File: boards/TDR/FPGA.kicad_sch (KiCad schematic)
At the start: 3 parts, among them U1 LFE5UM5G-45-CABGA381

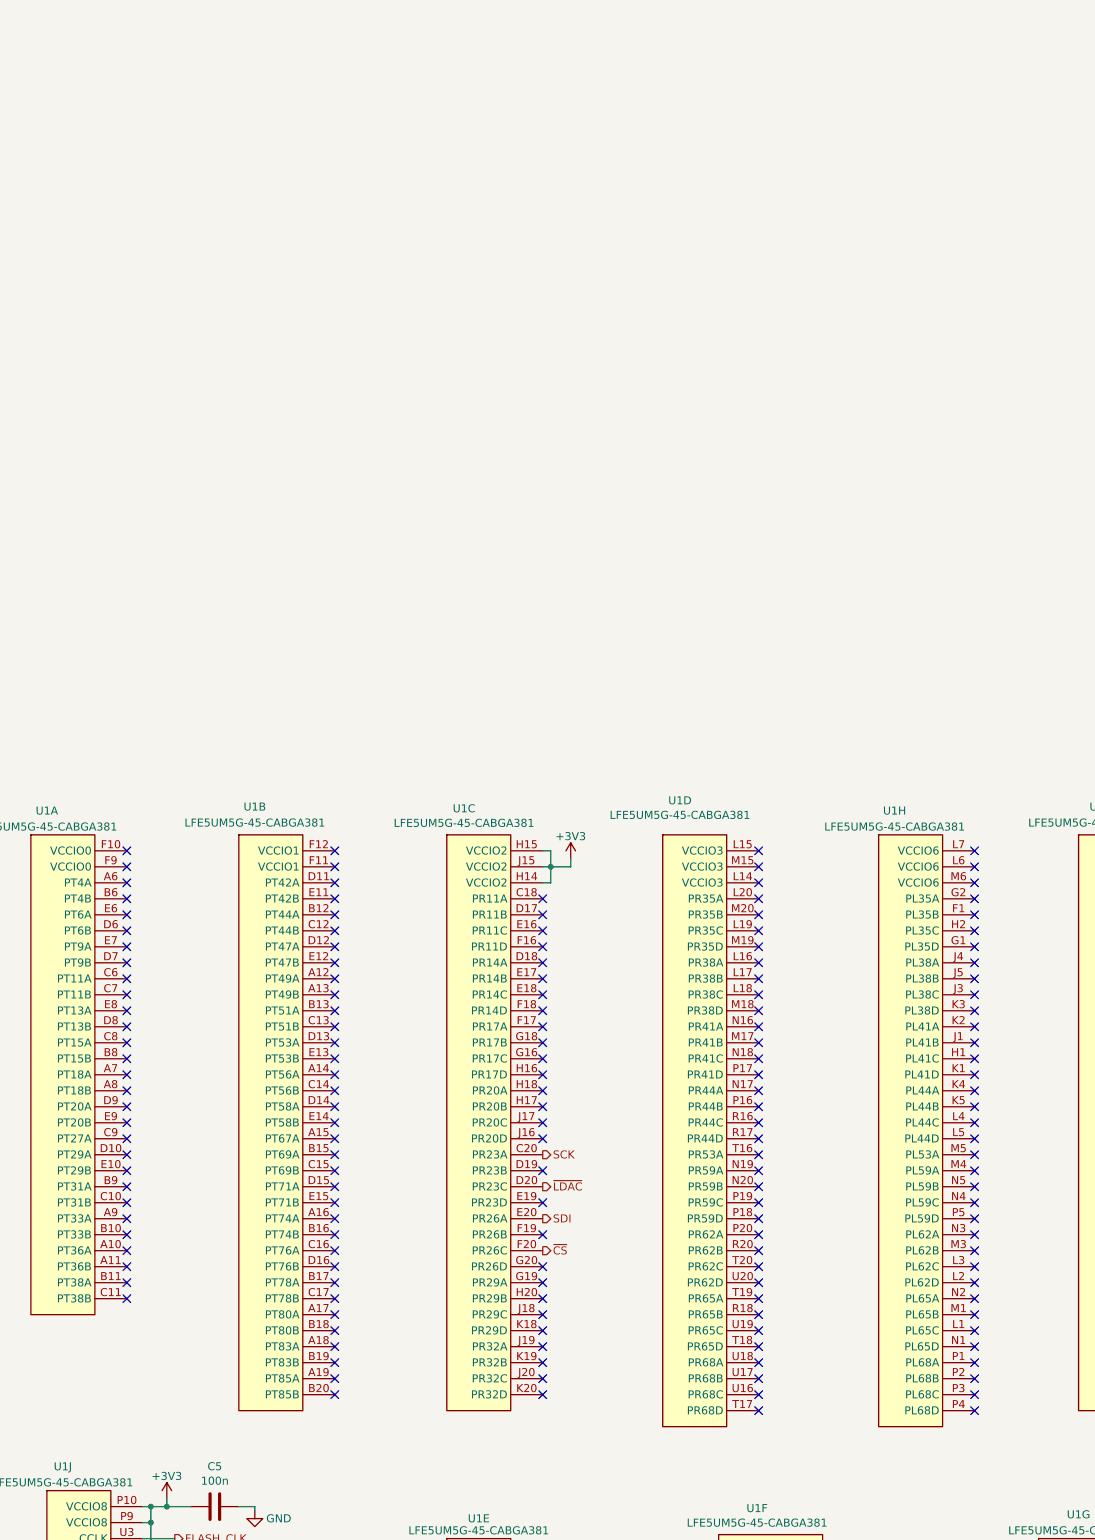
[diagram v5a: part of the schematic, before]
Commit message: add LEDs, only 9 unconnected items remaining
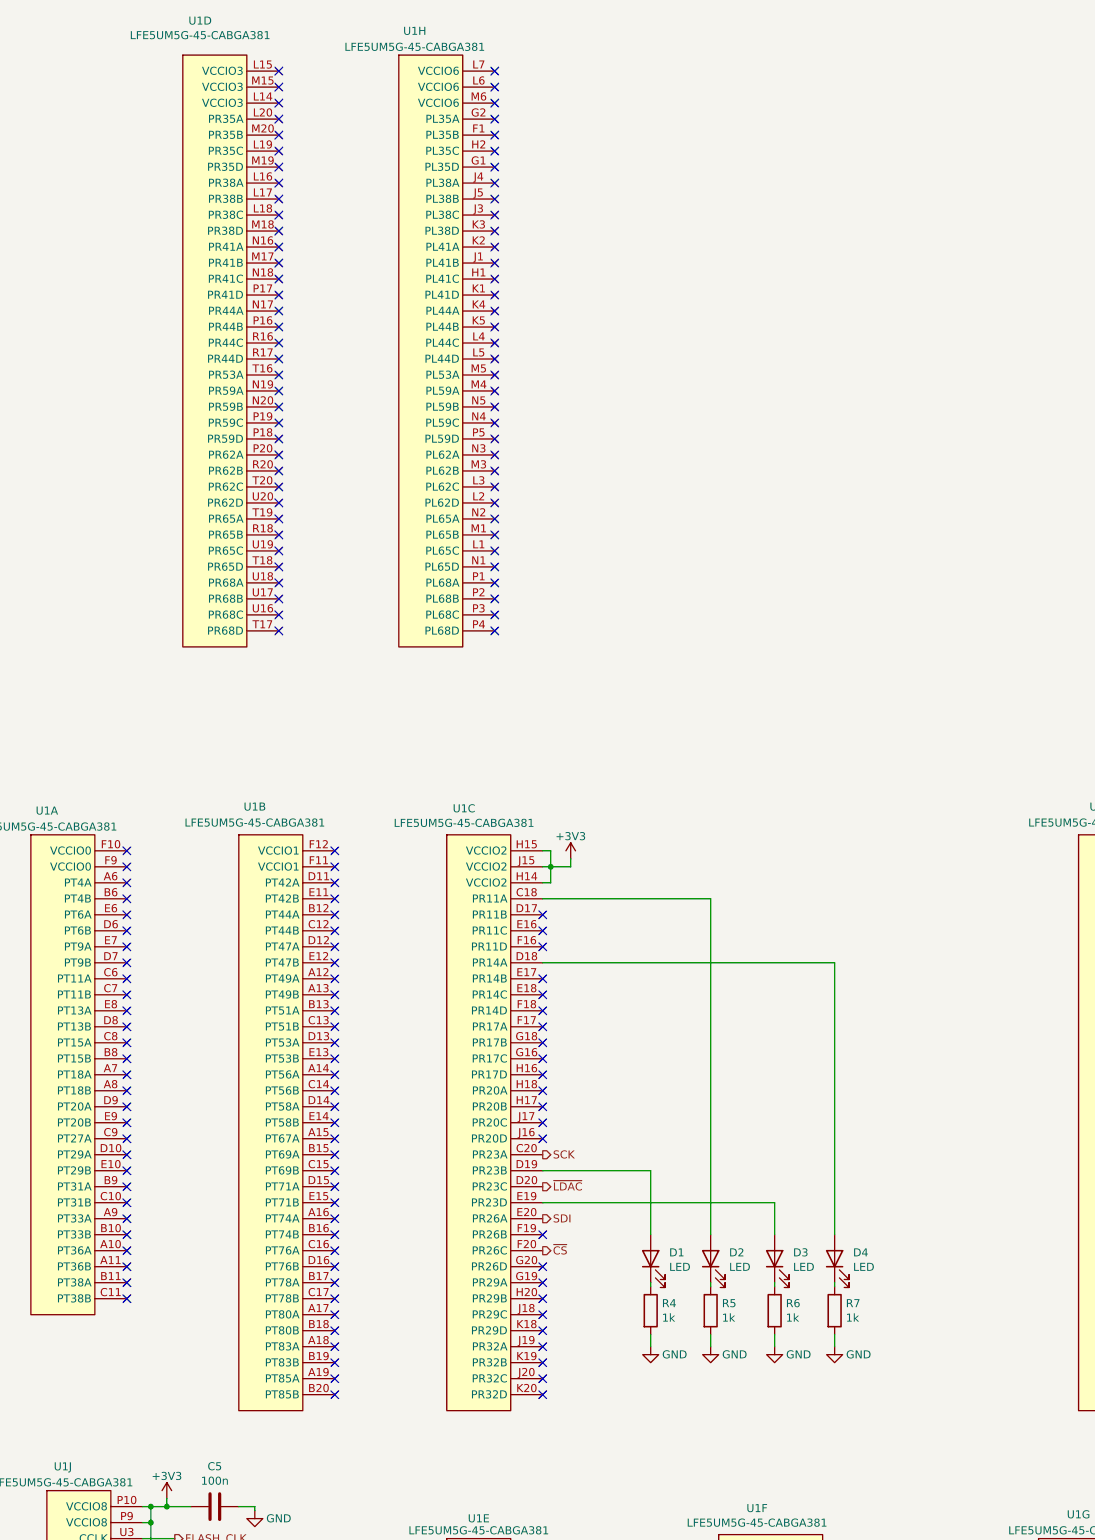
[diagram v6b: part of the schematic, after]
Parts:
- added D1, D2, D3, D4: LED, LED_SMD:LED_0805_2012Metric_Castellated, symbol Device:LED
- added R4, R5, R6, R7: 1k, Resistor_SMD:R_0805_2012Metric, symbol Device:R
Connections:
- net GND: now also R4.2, R5.2, R6.2, R7.2
- net at U1.C18 (PR11A): now also D2.2 (A)
- net at U1.D18 (PR14A): now also D4.2 (A)
- net at U1.D19 (PR23B): now also D1.2 (A)
- net at U1.E19 (PR23D): now also D3.2 (A)
- new net: D2.1 (K), R5.1
- new net: D1.1 (K), R4.1
- new net: D4.1 (K), R7.1
- new net: D3.1 (K), R6.1
- no-connect marks 201 -> 197
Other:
- moved on the sheet: U1D, U1H

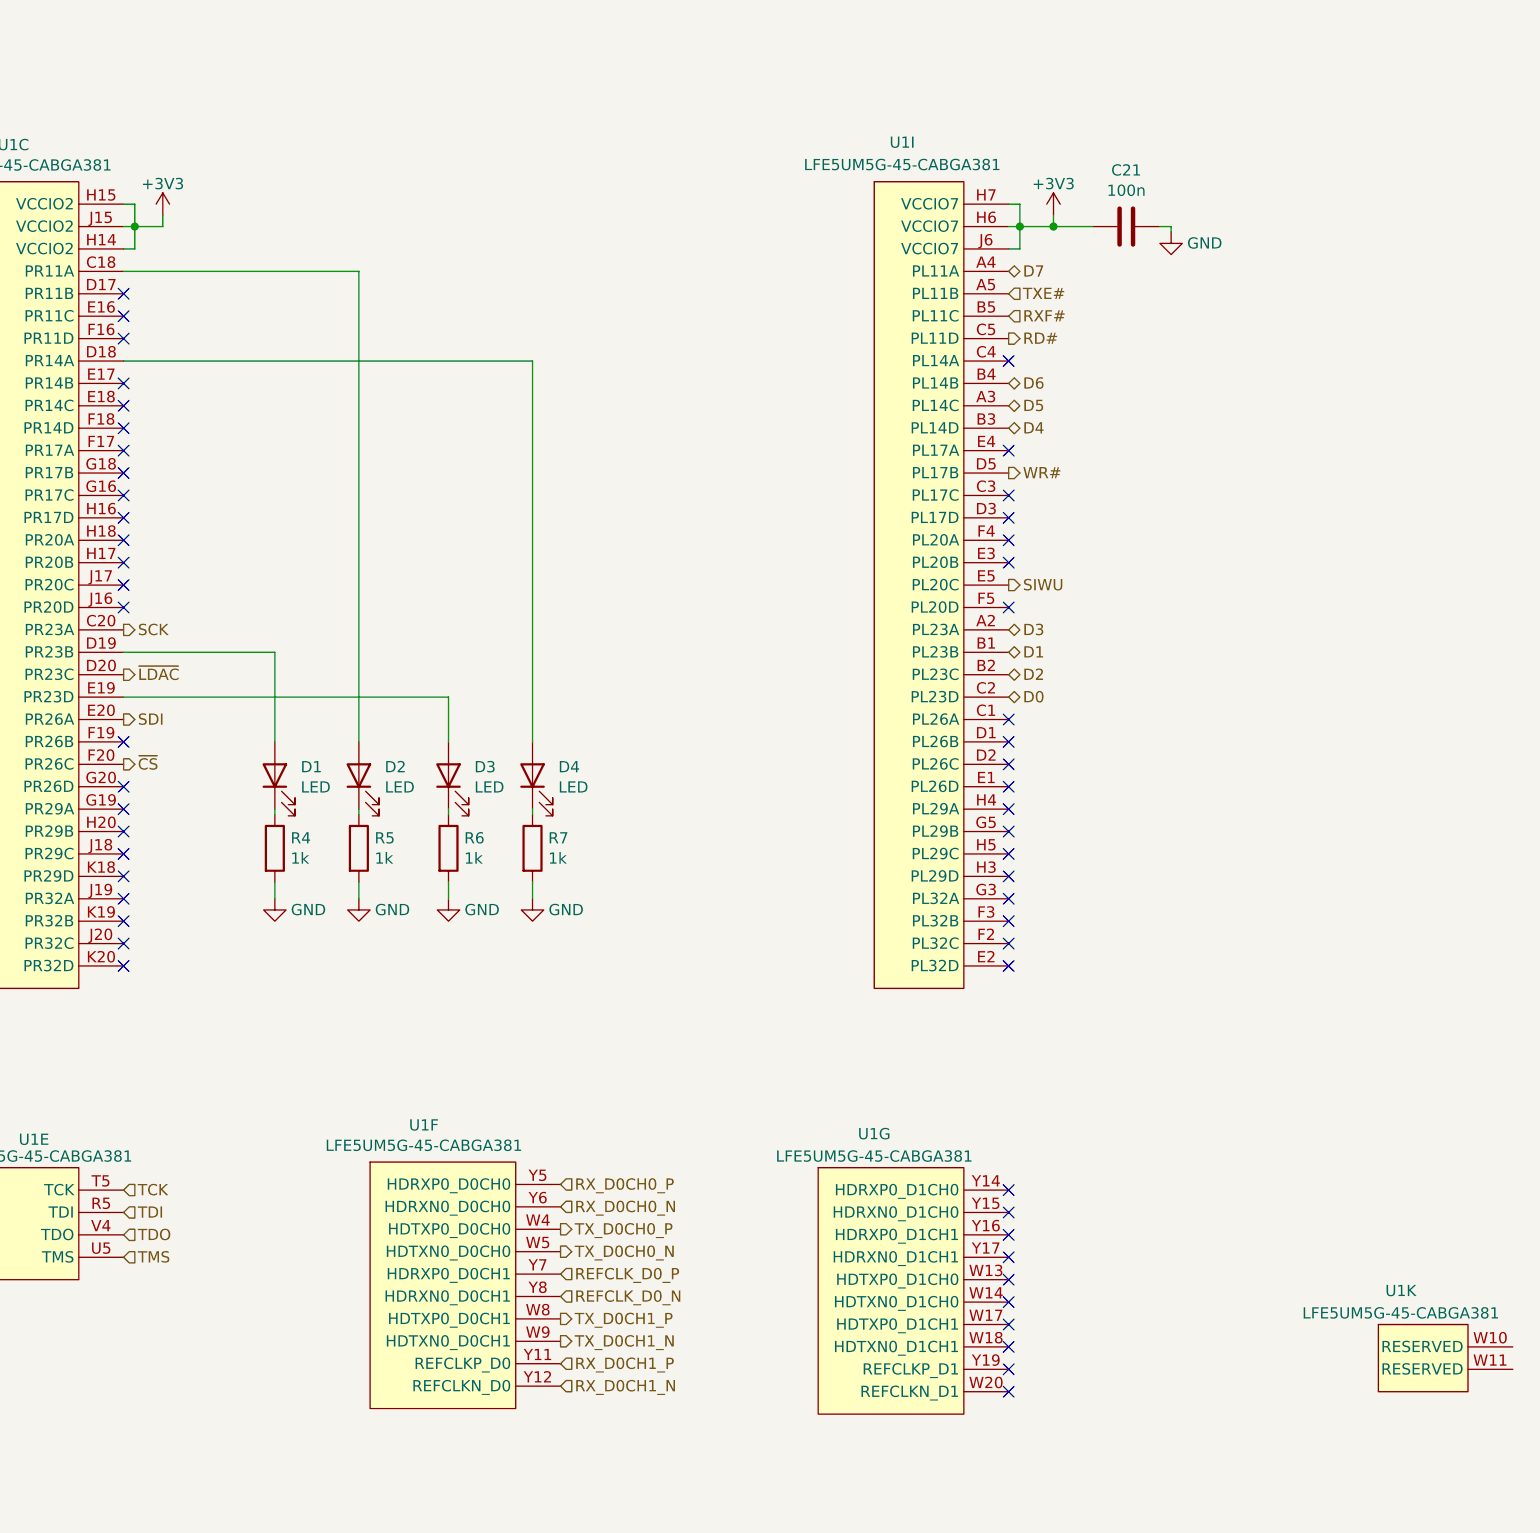
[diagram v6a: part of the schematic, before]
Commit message: finishing touches on the silkscreen
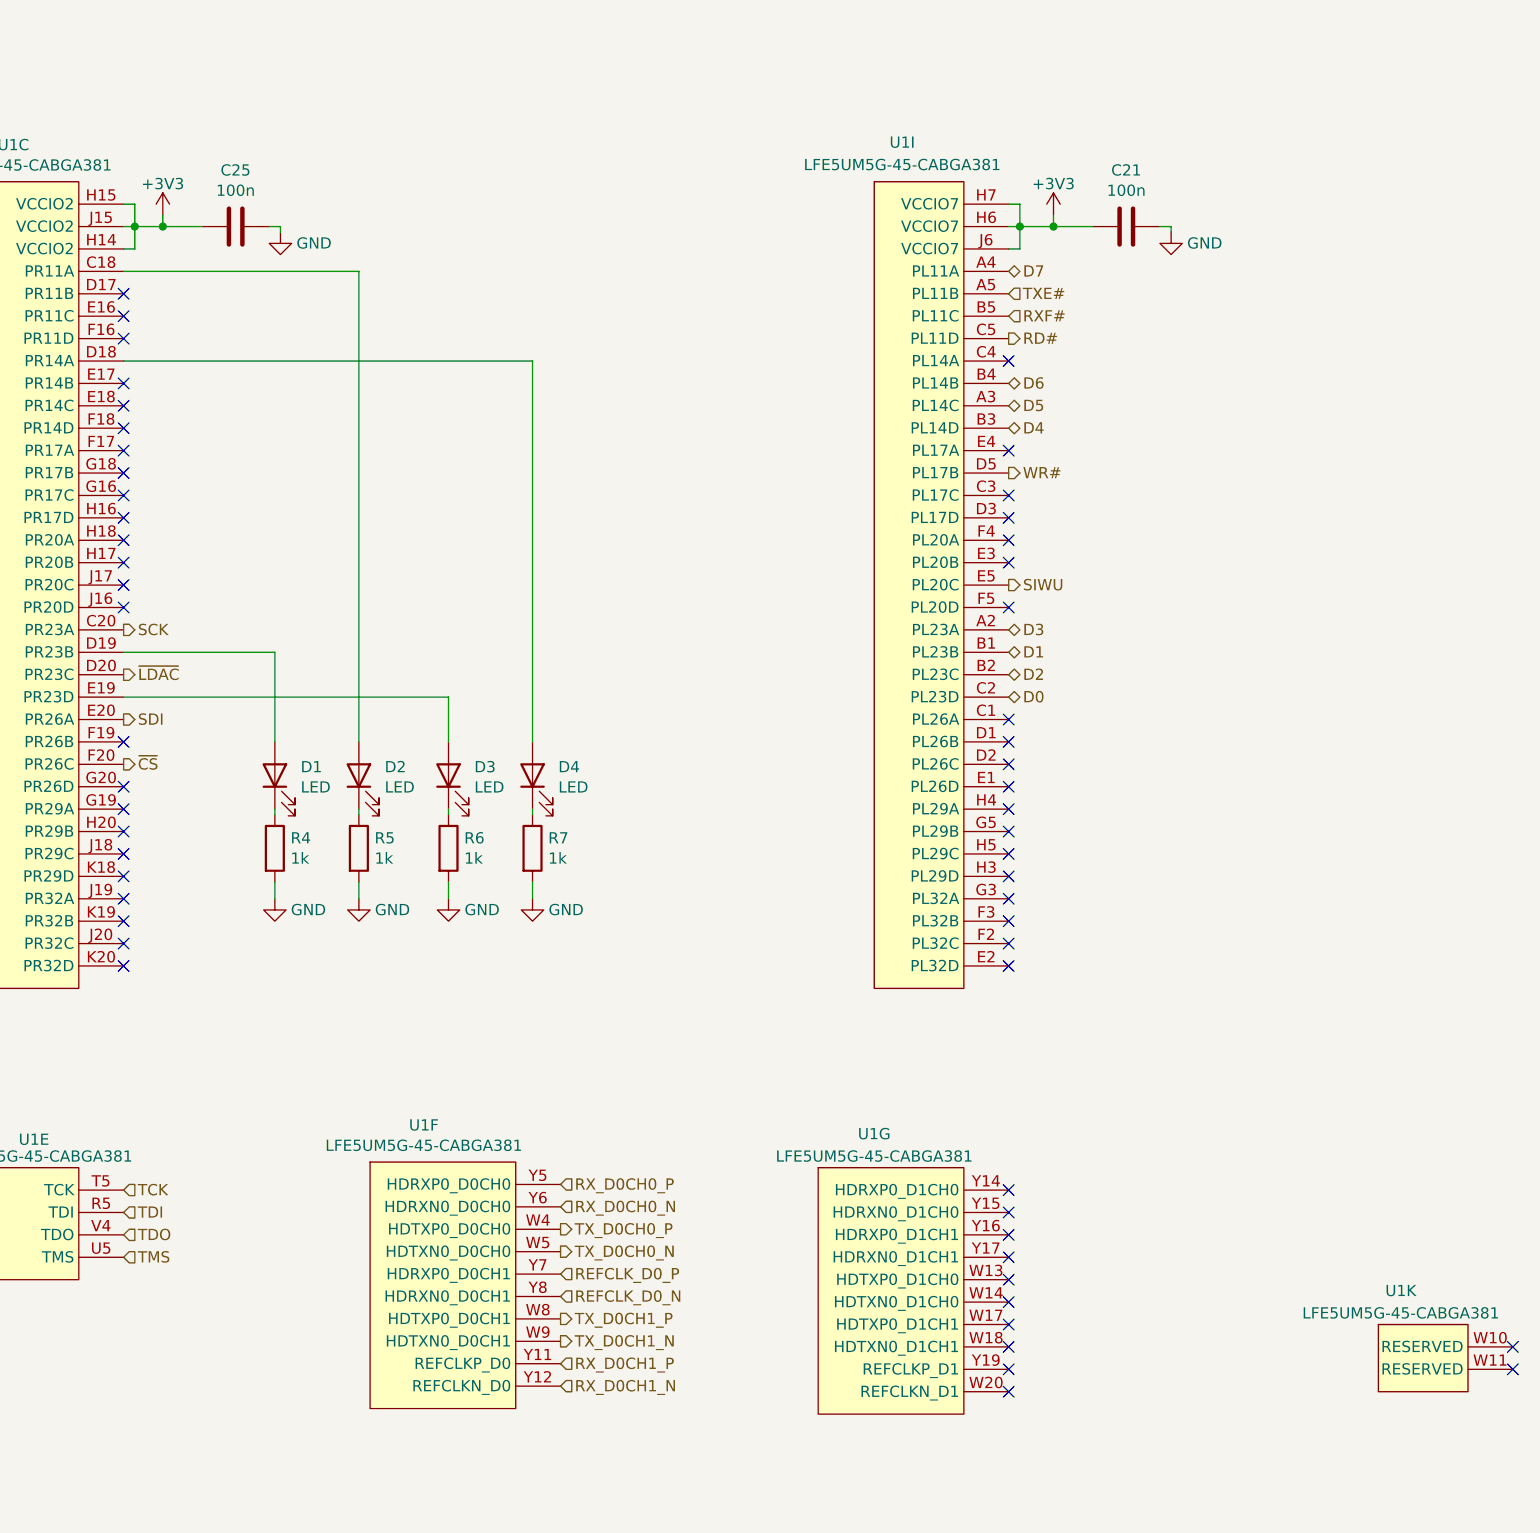
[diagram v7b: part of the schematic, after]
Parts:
- added C25: 100n, Capacitor_SMD:C_0402_1005Metric, symbol Device:C
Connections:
- net +3V3: now also C25.1
- net GND: now also C25.2
- no-connect marks 197 -> 199
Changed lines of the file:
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@@
   (junction (at 55.88 130.81) (diameter 0) (color 0 0 0 0))
   (junction (at 116.84 29.21) (diameter 0) (color 0 0 0 0))
+  (junction (at 120.015 29.21) (diameter 0) (color 0 0 0 0))
   (junction (at 217.17 29.21) (diameter 0) (color 0 0 0 0))
   (junction (at 220.98 29.21) (diameter 0) (color 0 0 0 0))
@@
   (no_connect (at 215.9 72.39))
   (no_connect (at 215.9 85.09))
+  (no_connect (at 273.05 156.21))
+  (no_connect (at 273.05 158.75))
   (no_connect (at 49.53 26.67))
   (no_connect (at 115.57 36.83))
@@
     (stroke (width 0) (type solid) (color 0 0 0 0))
   )
+  (wire (pts (xy 120.015 29.21) (xy 124.46 29.21))
+    (stroke (width 0) (type solid) (color 0 0 0 0))
+  )
+  (wire (pts (xy 132.08 29.21) (xy 133.35 29.21))
+    (stroke (width 0) (type solid) (color 0 0 0 0))
+  )
   (wire (pts (xy 132.715 77.47) (xy 132.715 87.63))
     (stroke (width 0) (type solid) (color 0 0 0 0))
@@
   )
   (wire (pts (xy 132.715 103.505) (xy 132.715 105.41))
+    (stroke (width 0) (type solid) (color 0 0 0 0))
+  )
+  (wire (pts (xy 133.35 29.21) (xy 133.35 29.845))
     (stroke (width 0) (type solid) (color 0 0 0 0))
   )
@@
     )
     (property "Datasheet" "" (id 3) (at 132.715 105.41 0)
+      (effects (font (size 1.27 1.27)) hide)
+    )
+  )
+  (symbol (lib_id "power:GND") (at 133.35 29.845 0) (unit 1)
+    (in_bom yes) (on_board yes)
+    (property "Reference" "#PWR0159" (id 0) (at 133.35 36.195 0)
+      (effects (font (size 1.27 1.27)) hide)
+    )
+    (property "Value" "GND" (id 1) (at 137.16 31.115 0))
+    (property "Footprint" "" (id 2) (at 133.35 29.845 0)
+      (effects (font (size 1.27 1.27)) hide)
+    )
+    (property "Datasheet" "" (id 3) (at 133.35 29.845 0)
       (effects (font (size 1.27 1.27)) hide)
     )
@@
       (effects (font (size 1.27 1.27)) hide)
     )
+  )
+  (symbol (lib_id "Device:C") (at 128.27 29.21 90) (unit 1)
+    (in_bom yes) (on_board yes)
+    (property "Reference" "C25" (id 0) (at 128.27 22.8408 90))
+    (property "Value" "100n" (id 1) (at 128.27 25.1395 90))
+    (property "Footprint" "Capacitor_SMD:C_0402_1005Metric" (id 2) (at 132.08 28.2448 0)
+      (effects (font (size 1.27 1.27)) hide)
+    )
+    (property "Datasheet" "~" (id 3) (at 128.27 29.21 0)
+      (effects (font (size 1.27 1.27)) hide)
+    )

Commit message: hopefully PCB is done
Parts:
- added TP1: TestPoint, TestPoint:TestPoint_Pad_D1.0mm, symbol Connector:TestPoint
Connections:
- net at U1.Y3 (DONE): now also TP1.1
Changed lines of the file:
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@@
+    (stroke (width 0) (type solid) (color 0 0 0 0))
+  )
+  (wire (pts (xy 52.07 146.05) (xy 60.96 146.05))
     (stroke (width 0) (type solid) (color 0 0 0 0))
   )
@@
     (effects (font (size 1.27 1.27)) (justify left))
   )
+  (symbol (lib_id "Connector:TestPoint") (at 60.96 146.05 270) (unit 1)
+    (in_bom yes) (on_board yes)
+    (property "Reference" "TP1" (id 0) (at 65.6591 144.9006 90)
+      (effects (font (size 1.27 1.27)) (justify left))
+    )
+    (property "Value" "TestPoint" (id 1) (at 65.6591 147.1993 90)
+      (effects (font (size 1.27 1.27)) (justify left))
+    )
+    (property "Footprint" "TestPoint:TestPoint_Pad_D1.0mm" (id 2) (at 60.96 151.13 0)
+      (effects (font (size 1.27 1.27)) hide)
+    )
+    (property "Datasheet" "~" (id 3) (at 60.96 151.13 0)
+      (effects (font (size 1.27 1.27)) hide)
+    )
+  )
   (symbol (lib_id "power:+3V3") (at 55.88 129.54 0) (unit 1)
